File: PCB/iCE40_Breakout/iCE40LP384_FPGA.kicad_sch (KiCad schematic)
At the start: 28 parts, among them Q1 L2N7002SLLT1G, SW1 KH-6X6X5H-STM, U1 ICE40LP384-SG32

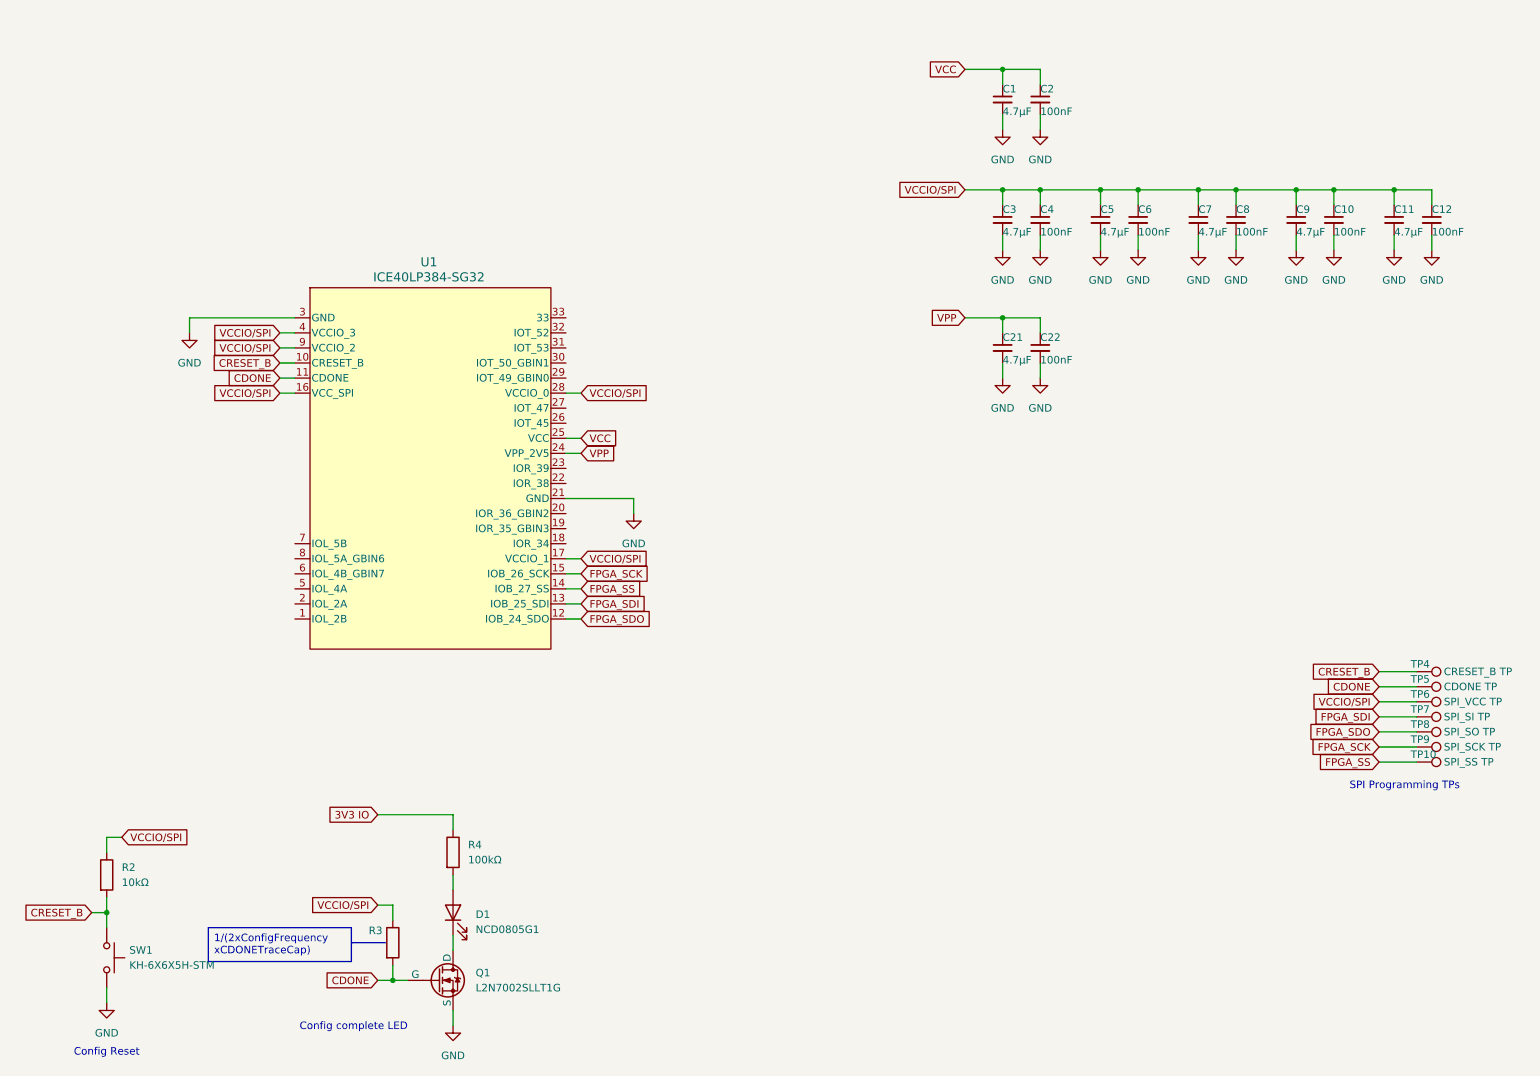
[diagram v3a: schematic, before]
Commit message: Wired FTDI chip to flash memory, and added power connections
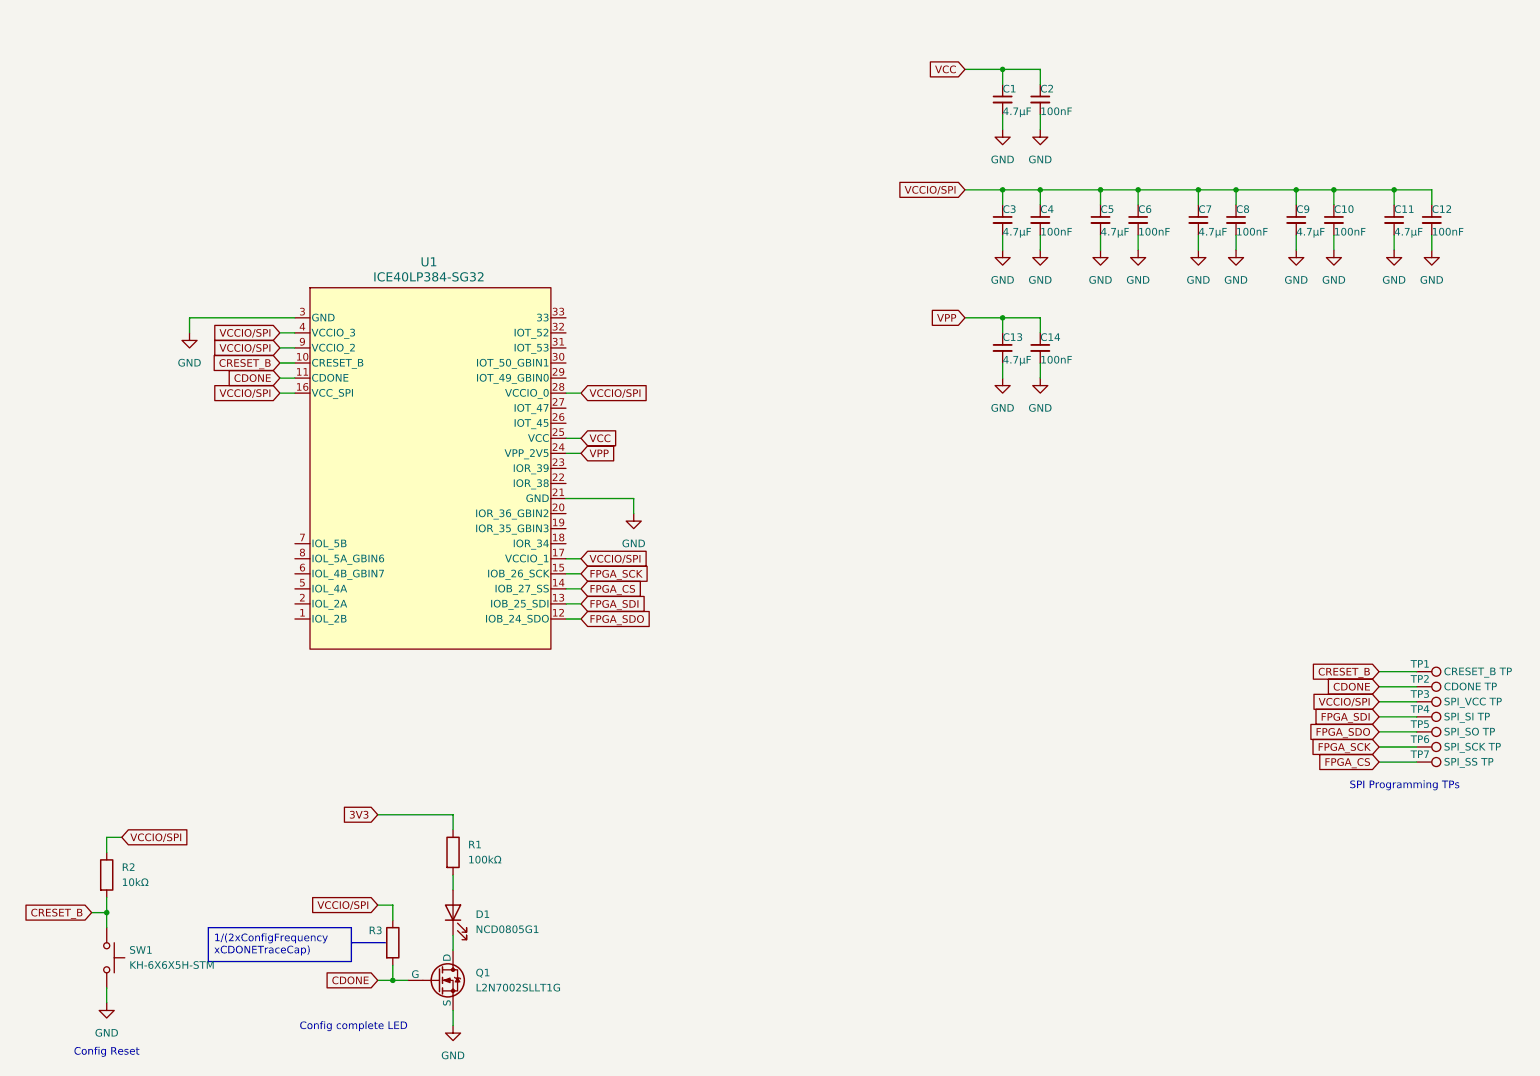
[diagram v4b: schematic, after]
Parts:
- renumbered C21 to C13, C22 to C14, R4 to R1, TP4 to TP1, TP5 to TP2, TP6 to TP3, TP7 to TP4, TP8 to TP5, TP9 to TP6, TP10 to TP7
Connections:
- net 3V3 IO renamed 3V3
- net FPGA_SS renamed FPGA_CS
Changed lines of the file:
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@@
 		)
 	)
-	(global_label "FPGA_SS"
+	(global_label "FPGA_CS"
 		(shape input)
 		(at 114.3 116.84 0)
@@
 		)
 	)
-	(global_label "3V3 IO"
+	(global_label "3V3"
 		(shape input)
 		(at 80.01 154.94 180)
@@
 		)
 		(property "Intersheetrefs" "${INTERSHEET_REFS}"
-			(at 70.6143 154.94 0)
+			(at 73.5172 154.94 0)
 			(effects
 				(font
@@
 		)
 	)
-	(global_label "FPGA_SS"
+	(global_label "FPGA_CS"
 		(shape input)
 		(at 248.92 146.05 180)
@@
 		(dnp no)
 		(fields_autoplaced yes)
-		(property "Reference" "#PWR020"
+		(property "Reference" "#PWR014"
 			(at 185.42 87.63 0)
 			(effects
@@
 			(project "iCE40_Breakout"
 				(path "/ce4d7974-ef38-4eea-8119-381c4298ef02/64261fd1-1565-42f1-91bd-c3aa9c264fe7"
-					(reference "#PWR020")
+					(reference "#PWR014")
 					(unit 1)
 				)
@@
 		(on_board yes)
 		(dnp no)
-		(property "Reference" "TP4"
+		(property "Reference" "TP1"
 			(at 254.254 129.54 90)
 			(effects
@@
 			(project ""
 				(path "/ce4d7974-ef38-4eea-8119-381c4298ef02/64261fd1-1565-42f1-91bd-c3aa9c264fe7"
-					(reference "TP4")
+					(reference "TP1")
 					(unit 1)
 				)
@@
 		(on_board yes)
 		(dnp no)
-		(property "Reference" "C21"
+		(property "Reference" "C13"
 			(at 185.42 74.422 0)
 			(effects
@@
 			(project "iCE40_Breakout"
 				(path "/ce4d7974-ef38-4eea-8119-381c4298ef02/64261fd1-1565-42f1-91bd-c3aa9c264fe7"
-					(reference "C21")
+					(reference "C13")
 					(unit 1)
 				)
@@
 		(dnp no)
 		(fields_autoplaced yes)
-		(property "Reference" "#PWR011"
+		(property "Reference" "#PWR09"
 			(at 234.95 66.04 0)
 			(effects
@@
 			(project "iCE40_Breakout"
 				(path "/ce4d7974-ef38-4eea-8119-381c4298ef02/64261fd1-1565-42f1-91bd-c3aa9c264fe7"
-					(reference "#PWR011")
+					(reference "#PWR09")
 					(unit 1)
 				)
@@
 		(on_board yes)
 		(dnp no)
-		(property "Reference" "C22"
+		(property "Reference" "C14"
 			(at 191.77 74.422 0)
 			(effects
@@
 			(project "iCE40_Breakout"
 				(path "/ce4d7974-ef38-4eea-8119-381c4298ef02/64261fd1-1565-42f1-91bd-c3aa9c264fe7"
-					(reference "C22")
+					(reference "C14")
 					(unit 1)
 				)
@@
 		(on_board yes)
 		(dnp no)
-		(property "Reference" "#PWR08"
+		(property "Reference" "#PWR06"
 			(at 208.28 66.04 0)
 			(effects
@@
 			(project "iCE40_Breakout"
 				(path "/ce4d7974-ef38-4eea-8119-381c4298ef02/64261fd1-1565-42f1-91bd-c3aa9c264fe7"
-					(reference "#PWR08")
+					(reference "#PWR06")
 					(unit 1)
 				)
@@
 		(dnp no)
 		(fields_autoplaced yes)
-		(property "Reference" "#PWR06"
+		(property "Reference" "#PWR04"
 			(at 191.77 66.04 0)
 			(effects
@@
 			(project "iCE40_Breakout"
 				(path "/ce4d7974-ef38-4eea-8119-381c4298ef02/64261fd1-1565-42f1-91bd-c3aa9c264fe7"
-					(reference "#PWR06")
+					(reference "#PWR04")
 					(unit 1)
 				)
@@
 		(dnp no)
 		(fields_autoplaced yes)
-		(property "Reference" "#PWR03"
+		(property "Reference" "#PWR013"
 			(at 48.26 80.01 0)
 			(effects
@@
 			(project "iCE40_Breakout"
 				(path "/ce4d7974-ef38-4eea-8119-381c4298ef02/64261fd1-1565-42f1-91bd-c3aa9c264fe7"
-					(reference "#PWR03")
+					(reference "#PWR013")
 					(unit 1)
 				)
@@
 		(dnp no)
 		(fields_autoplaced yes)
-		(property "Reference" "#PWR010"
+		(property "Reference" "#PWR08"
 			(at 224.79 66.04 0)
 			(effects
@@
 			(project "iCE40_Breakout"
 				(path "/ce4d7974-ef38-4eea-8119-381c4298ef02/64261fd1-1565-42f1-91bd-c3aa9c264fe7"
-					(reference "#PWR010")
+					(reference "#PWR08")
 					(unit 1)
 				)
@@
 		(dnp no)
 		(fields_autoplaced yes)
-		(property "Reference" "#PWR04"
+		(property "Reference" "#PWR016"
 			(at 123.19 110.49 0)
 			(effects
@@
 			(project "iCE40_Breakout"
 				(path "/ce4d7974-ef38-4eea-8119-381c4298ef02/64261fd1-1565-42f1-91bd-c3aa9c264fe7"
-					(reference "#PWR04")
+					(reference "#PWR016")
 					(unit 1)
 				)
@@
 		(dnp no)
 		(fields_autoplaced yes)
-		(property "Reference" "#PWR021"
+		(property "Reference" "#PWR015"
 			(at 191.77 87.63 0)
 			(effects
@@
 			(project "iCE40_Breakout"
 				(path "/ce4d7974-ef38-4eea-8119-381c4298ef02/64261fd1-1565-42f1-91bd-c3aa9c264fe7"
-					(reference "#PWR021")
+					(reference "#PWR015")
 					(unit 1)
 				)
@@
 		(dnp no)
 		(fields_autoplaced yes)
-		(property "Reference" "#PWR09"
+		(property "Reference" "#PWR07"
 			(at 218.44 66.04 0)
 			(effects
@@
 			(project "iCE40_Breakout"
 				(path "/ce4d7974-ef38-4eea-8119-381c4298ef02/64261fd1-1565-42f1-91bd-c3aa9c264fe7"
-					(reference "#PWR09")
+					(reference "#PWR07")
 					(unit 1)
 				)
@@
 		(on_board yes)
 		(dnp no)
-		(property "Reference" "TP6"
+		(property "Reference" "TP3"
 			(at 254.254 134.62 90)
 			(effects
@@
 			(project "iCE40_Breakout"
 				(path "/ce4d7974-ef38-4eea-8119-381c4298ef02/64261fd1-1565-42f1-91bd-c3aa9c264fe7"
-					(reference "TP6")
+					(reference "TP3")
 					(unit 1)
 				)
@@
 		(on_board yes)
 		(dnp no)
-		(property "Reference" "TP8"
+		(property "Reference" "TP5"
 			(at 254.254 139.7 90)
 			(effects
@@
 			(project "iCE40_Breakout"
 				(path "/ce4d7974-ef38-4eea-8119-381c4298ef02/64261fd1-1565-42f1-91bd-c3aa9c264fe7"
-					(reference "TP8")
+					(reference "TP5")
 					(unit 1)
 				)
@@
 		(on_board yes)
 		(dnp no)
-		(property "Reference" "TP7"
+		(property "Reference" "TP4"
 			(at 254.254 137.16 90)
 			(effects
@@
 			(project "iCE40_Breakout"
 				(path "/ce4d7974-ef38-4eea-8119-381c4298ef02/64261fd1-1565-42f1-91bd-c3aa9c264fe7"
-					(reference "TP7")
+					(reference "TP4")
 					(unit 1)
 				)
@@
 		(dnp no)
 		(fields_autoplaced yes)
-		(property "Reference" "#PWR012"
+		(property "Reference" "#PWR010"
 			(at 241.3 66.04 0)
 			(effects
@@
 			(project "iCE40_Breakout"
 				(path "/ce4d7974-ef38-4eea-8119-381c4298ef02/64261fd1-1565-42f1-91bd-c3aa9c264fe7"
-					(reference "#PWR012")
+					(reference "#PWR010")
 					(unit 1)
 				)
@@
 		(dnp no)
 		(fields_autoplaced yes)
-		(property "Reference" "#PWR07"
+		(property "Reference" "#PWR05"
 			(at 201.93 66.04 0)
 			(effects
@@
 			(project "iCE40_Breakout"
 				(path "/ce4d7974-ef38-4eea-8119-381c4298ef02/64261fd1-1565-42f1-91bd-c3aa9c264fe7"
-					(reference "#PWR07")
+					(reference "#PWR05")
 					(unit 1)
 				)
@@
 		(dnp no)
 		(fields_autoplaced yes)
-		(property "Reference" "#PWR016"
+		(property "Reference" "#PWR017"
 			(at 34.29 193.04 0)
 			(effects
@@
 			(project "iCE40_Breakout"
 				(path "/ce4d7974-ef38-4eea-8119-381c4298ef02/64261fd1-1565-42f1-91bd-c3aa9c264fe7"
-					(reference "#PWR016")
+					(reference "#PWR017")
 					(unit 1)
 				)
@@
 		(on_board yes)
 		(dnp no)
-		(property "Reference" "TP10"
+		(property "Reference" "TP7"
 			(at 254.254 144.78 90)
 			(effects
@@
 			(project "iCE40_Breakout"
 				(path "/ce4d7974-ef38-4eea-8119-381c4298ef02/64261fd1-1565-42f1-91bd-c3aa9c264fe7"
-					(reference "TP10")
+					(reference "TP7")
 					(unit 1)
 				)
@@
 		(dnp no)
 		(fields_autoplaced yes)
-		(property "Reference" "R4"
+		(property "Reference" "R1"
 			(at 95.25 160.0199 0)
 			(effects
@@
 			(project ""
 				(path "/ce4d7974-ef38-4eea-8119-381c4298ef02/64261fd1-1565-42f1-91bd-c3aa9c264fe7"
-					(reference "R4")
+					(reference "R1")
 					(unit 1)
 				)
@@
 		(dnp no)
 		(fields_autoplaced yes)
-		(property "Reference" "#PWR014"
+		(property "Reference" "#PWR012"
 			(at 257.81 66.04 0)
 			(effects
@@
 			(project "iCE40_Breakout"
 				(path "/ce4d7974-ef38-4eea-8119-381c4298ef02/64261fd1-1565-42f1-91bd-c3aa9c264fe7"
-					(reference "#PWR014")
+					(reference "#PWR012")
 					(unit 1)
 				)
@@
 		(dnp no)
 		(fields_autoplaced yes)
-		(property "Reference" "#PWR013"
+		(property "Reference" "#PWR011"
 			(at 251.46 66.04 0)
 			(effects
@@
 			(project "iCE40_Breakout"
 				(path "/ce4d7974-ef38-4eea-8119-381c4298ef02/64261fd1-1565-42f1-91bd-c3aa9c264fe7"
-					(reference "#PWR013")
+					(reference "#PWR011")
 					(unit 1)
 				)
@@
 		(dnp no)
 		(fields_autoplaced yes)
-		(property "Reference" "#PWR022"
+		(property "Reference" "#PWR018"
 			(at 92.71 196.85 0)
 			(effects
@@
 			(project "iCE40_Breakout"
 				(path "/ce4d7974-ef38-4eea-8119-381c4298ef02/64261fd1-1565-42f1-91bd-c3aa9c264fe7"
-					(reference "#PWR022")
+					(reference "#PWR018")
 					(unit 1)
 				)
@@
 		(on_board yes)
 		(dnp no)
-		(property "Reference" "TP9"
+		(property "Reference" "TP6"
 			(at 254.254 142.24 90)
 			(effects
@@
 			(project "iCE40_Breakout"
 				(path "/ce4d7974-ef38-4eea-8119-381c4298ef02/64261fd1-1565-42f1-91bd-c3aa9c264fe7"
-					(reference "TP9")
+					(reference "TP6")
 					(unit 1)
 				)
@@
 		(on_board yes)
 		(dnp no)
-		(property "Reference" "TP5"
+		(property "Reference" "TP2"
 			(at 254.254 132.08 90)
 			(effects
@@
 			(project "iCE40_Breakout"
 				(path "/ce4d7974-ef38-4eea-8119-381c4298ef02/64261fd1-1565-42f1-91bd-c3aa9c264fe7"
-					(reference "TP5")
+					(reference "TP2")
 					(unit 1)
 				)
@@
 		(dnp no)
 		(fields_autoplaced yes)
-		(property "Reference" "#PWR05"
+		(property "Reference" "#PWR03"
 			(at 185.42 66.04 0)
 			(effects
@@
 			(project "iCE40_Breakout"
 				(path "/ce4d7974-ef38-4eea-8119-381c4298ef02/64261fd1-1565-42f1-91bd-c3aa9c264fe7"
-					(reference "#PWR05")
+					(reference "#PWR03")
 					(unit 1)
 				)

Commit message: Finished first draft of full schematic
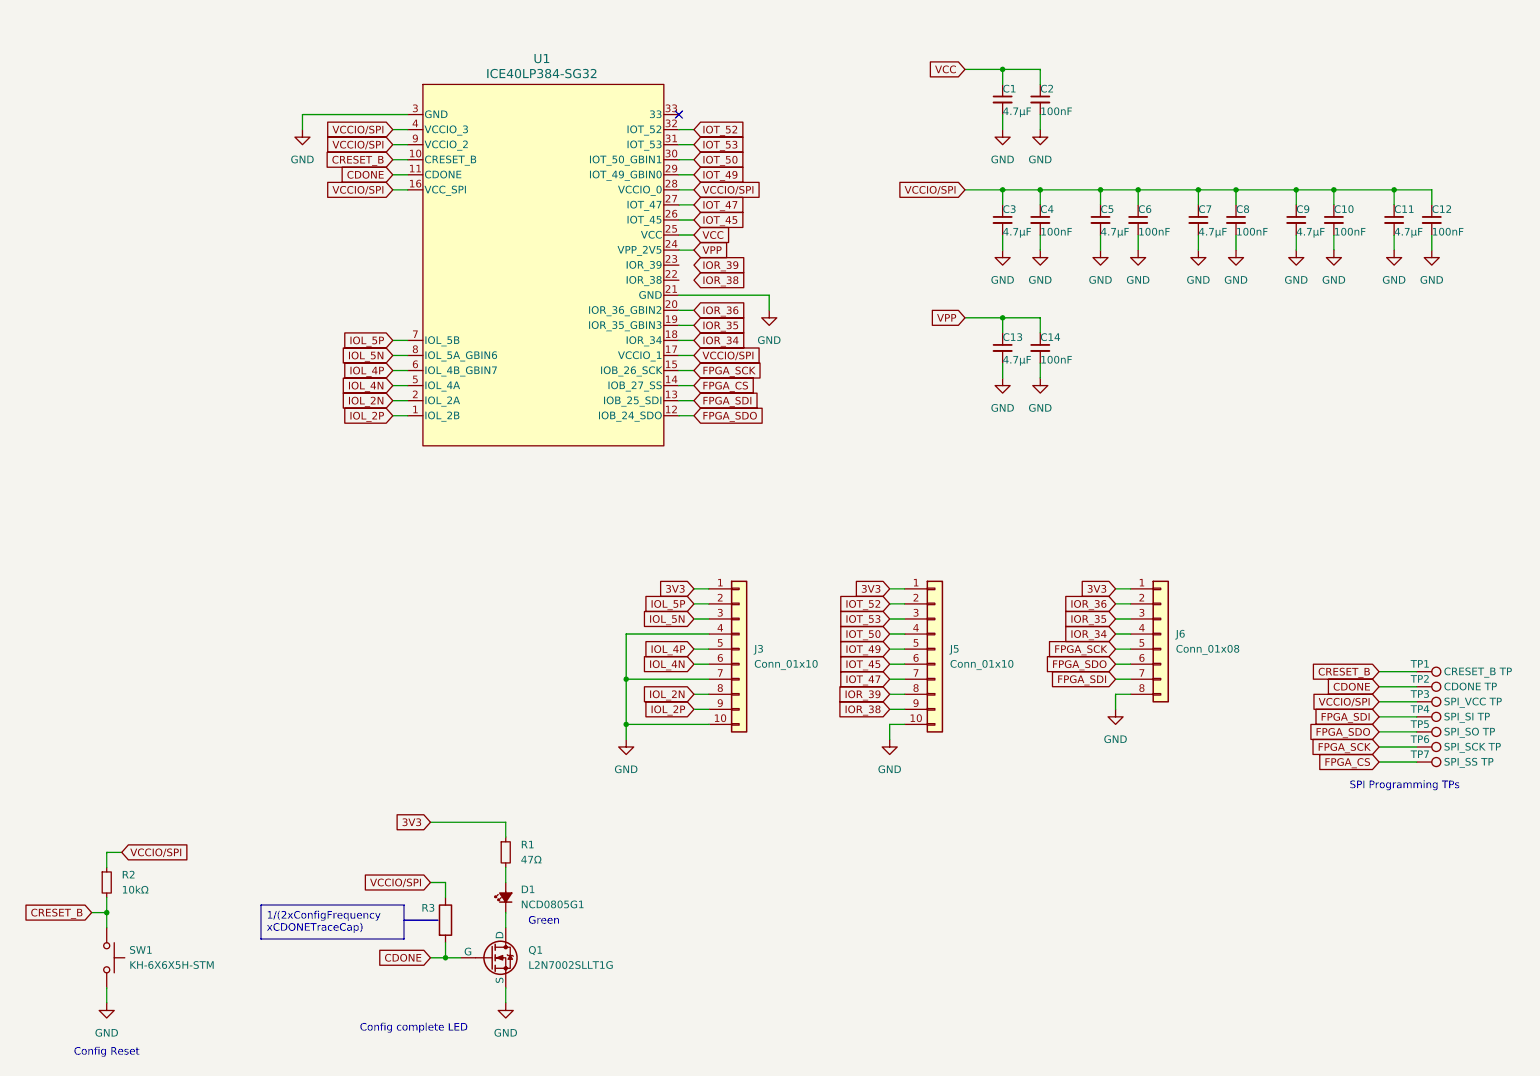
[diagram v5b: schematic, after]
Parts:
- added J3, J5: Conn_01x10, symbol Connector_Generic:Conn_01x10
- added J6: Conn_01x08, symbol Connector_Generic:Conn_01x08
- D1: symbol Device:LED -> Device:LED_Small_Filled
- R1: value 100kΩ -> 47Ω; symbol Device:R -> Device:R_Small; LCSC C25803 -> C23182
- R2: symbol Device:R -> Device:R_Small
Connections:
- net 3V3: now also J3.1 (Pin_1), J5.1 (Pin_1), J6.1 (Pin_1)
- net FPGA_SCK: now also J6.5 (Pin_5)
- net FPGA_SDI: now also J6.7 (Pin_7)
- net FPGA_SDO: now also J6.6 (Pin_6)
- net GND: now also J3.10 (Pin_10), J3.4 (Pin_4), J3.7 (Pin_7), J5.10 (Pin_10), J6.8 (Pin_8)
- net IOL_2P: now reaches U1.1 (IOL_2B)
- net IOL_2P: now also J3.9 (Pin_9)
- net IOR_34: now reaches U1.18 (IOR_34)
- net IOR_34: now also J6.4 (Pin_4)
- net IOR_35: now reaches U1.19 (IOR_35_GBIN3)
- net IOR_35: now also J6.3 (Pin_3)
- net IOL_2N: now reaches U1.2 (IOL_2A)
- net IOL_2N: now also J3.8 (Pin_8)
- net IOR_36: now reaches U1.20 (IOR_36_GBIN2)
- net IOR_36: now also J6.2 (Pin_2)
- net IOT_45: now reaches U1.26 (IOT_45)
- net IOT_45: now also J5.6 (Pin_6)
- net IOT_47: now reaches U1.27 (IOT_47)
- net IOT_47: now also J5.7 (Pin_7)
- net IOT_49: now reaches U1.29 (IOT_49_GBIN0)
- net IOT_49: now also J5.5 (Pin_5)
- net IOT_50: now reaches U1.30 (IOT_50_GBIN1)
- net IOT_50: now also J5.4 (Pin_4)
- net IOT_53: now reaches U1.31 (IOT_53)
- net IOT_53: now also J5.3 (Pin_3)
- net IOT_52: now reaches U1.32 (IOT_52)
- net IOT_52: now also J5.2 (Pin_2)
- net IOL_4N: now reaches U1.5 (IOL_4A)
- net IOL_4N: now also J3.6 (Pin_6)
- net IOL_4P: now reaches U1.6 (IOL_4B_GBIN7)
- net IOL_4P: now also J3.5 (Pin_5)
- net IOL_5P: now reaches U1.7 (IOL_5B)
- net IOL_5P: now also J3.2 (Pin_2)
- net IOL_5N: now reaches U1.8 (IOL_5A_GBIN6)
- net IOL_5N: now also J3.3 (Pin_3)
- new net IOR_38: J5.9 (Pin_9)
- new net IOR_39: J5.8 (Pin_8)
- no-connect marks 0 -> 1
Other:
- note added: "Green"
- moved on the sheet: Q1, R1, R2, R3, U1
